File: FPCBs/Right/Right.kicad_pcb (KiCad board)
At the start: 2 copper layers, 61.5 x 89.2 mm, 23 parts, among them J1 PCB, J5 2nd Focus+Shutter, J6 Conn_01x03_Pin, SW1 Mode Dial, SW2 ON/OFF, SW3 Focus+Shutter, SW4 Focus+Shutter, SW6 ON/OFF, U1 SG-105, U2 SG-105

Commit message: Fix the buttons pins
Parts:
- removed F1: Fuse, Leica-G9ii:R_2x1mm
- added R9: 5k, Leica-G9ii:R_2x1mm, F.Cu at (121.8, 114.5)
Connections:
- RV1 pad 2: Net-(J1-Pin_35) -> Net-(J1-Pin_34)
- RV1 pad 3: Net-(J1-Pin_34) -> Net-(J1-Pin_35)
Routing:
- net Net-(J1-Pin_34): track 83.1 -> 87.0 mm
- net Net-(J1-Pin_35): track 85.7 -> 83.5 mm
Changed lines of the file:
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@@
 		)
 	)
+	(footprint "Leica-G9ii:R_2x1mm"
+		(layer "F.Cu")
+		(at 121.81 114.5 90)
+		(descr "Resistor SMD 0603 (1608 Metric), square (rectangular) end terminal, IPC-7351 nominal, (Body size source: IPC-SM-782 page 72, https://www.pcb-3d.com/wordpress/wp-content/uploads/ipc-sm-782a_amendment_1_and_2.pdf), generated with kicad-footprint-generator")
+		(tags "resistor")
+		(property "Reference" "R9"
+			(at 0 -1.43 90)
+			(layer "F.SilkS")
+			(hide yes)
+			(effects
+				(font
+					(size 1 1)
+					(thickness 0.15)
+				)
+			)
+		)
+		(property "Value" "5k"
+			(at 0 1.43 90)
+			(layer "F.Fab")
+			(effects
+				(font
+					(size 1 1)
+					(thickness 0.15)
+				)
+			)
+		)
+		(property "Datasheet" "~"
+			(at 0 0 90)
+			(layer "F.Fab")
+			(hide yes)
+			(effects
+				(font
+					(size 1.27 1.27)
+					(thickness 0.15)
+				)
+			)
+		)
+		(property "Description" "Resistor"
+			(at 0 0 90)
+			(layer "F.Fab")
+			(hide yes)
+			(effects
+				(font
+					(size 1.27 1.27)
+					(thickness 0.15)
+				)
+			)
+		)
+		(property ki_fp_filters "R_*")
+		(sheetname "/")
+		(sheetfile "Right.kicad_sch")
+		(attr smd)
+		(fp_rect
+			(start -1 -0.5)
+			(end 1 0.5)
+			(stroke
+				(width 0.05)
+				(type solid)
+			)
+			(fill no)
+			(layer "F.CrtYd")
+		)
+		(fp_line
+			(start 0.8 -0.4125)
+			(end 0.8 0.4125)
+			(stroke
+				(width 0.1)
+				(type solid)
+			)
+			(layer "F.Fab")
+		)
+		(fp_line
+			(start -0.8 -0.4125)
+			(end 0.8 -0.4125)
+			(stroke
+				(width 0.1)
+				(type solid)
+			)
+			(layer "F.Fab")
+		)
+		(fp_line
+			(start 0.8 0.4125)
+			(end -0.8 0.4125)
+			(stroke
+				(width 0.1)
+				(type solid)
+			)
+			(layer "F.Fab")
+		)
+		(fp_line
+			(start -0.8 0.4125)
+			(end -0.8 -0.4125)
+			(stroke
+				(width 0.1)
+				(type solid)
+			)
+			(layer "F.Fab")
+		)
+		(fp_text user "${REFERENCE}"
+			(at 3.42 0 90)
+			(layer "F.Fab")
+			(effects
+				(font
+					(size 0.4 0.4)
+					(thickness 0.06)
+				)
+			)
+		)
+		(pad "" smd roundrect
+			(at -0.6 0 90)
+			(size 0.6 0.8)
+			(layers "F.Mask" "F.Paste")
+			(roundrect_rratio 0.25)
+		)
+		(pad "" smd roundrect
+			(at 0.61 0 90)
+			(size 0.6 0.8)
+			(layers "F.Mask" "F.Paste")
+			(roundrect_rratio 0.25)
+		)
+		(pad "1" smd roundrect
+			(at -0.6 0 90)
+			(size 0.8 1)
+			(layers "F.Cu")
+			(roundrect_rratio 0.25)
+			(net 6 "Net-(J1-Pin_31)")
+			(pintype "passive")
+		)
+		(pad "2" smd roundrect
+			(at 0.6 0 90)
+			(size 0.8 1)
+			(layers "F.Cu")
+			(roundrect_rratio 0.25)
+			(net 5 "Net-(BT1-+)")
+			(pintype "passive")
+		)
+		(embedded_fonts no)
+		(model "${KICAD9_3DMODEL_DIR}/Resistor_SMD.3dshapes/R_0603_1608Metric.step"
+			(offset
+				(xyz 0 0 0)
+			)
+			(scale
+				(xyz 1 1 1)
+			)
+			(rotate
+				(xyz 0 0 0)
+			)
+		)
+	)
 	(footprint "Leica-G9ii:Battery_Cell"
 		(layer "F.Cu")
@@
 		)
 	)
-	(footprint "Leica-G9ii:R_2x1mm"
-		(layer "F.Cu")
-		(at 121.82 114.47 90)
-		(descr "Resistor SMD 0603 (1608 Metric), square (rectangular) end terminal, IPC-7351 nominal, (Body size source: IPC-SM-782 page 72, https://www.pcb-3d.com/wordpress/wp-content/uploads/ipc-sm-782a_amendment_1_and_2.pdf), generated with kicad-footprint-generator")
-		(tags "resistor")
-		(property "Reference" "F1"
-			(at 0 -1.43 90)
-			(layer "F.SilkS")
-			(hide yes)
-			(effects
-				(font
-					(size 1 1)
-					(thickness 0.15)
-				)
-			)
-		)
-		(property "Value" "Fuse"
-			(at 0 1.43 90)
-			(layer "F.Fab")
-			(effects
-				(font
-					(size 1 1)
-					(thickness 0.15)
-				)
-			)
-		)
-		(property "Datasheet" "~"
-			(at 0 0 90)
-			(layer "F.Fab")
-			(hide yes)
-			(effects
-				(font
-					(size 1.27 1.27)
-					(thickness 0.15)
-				)
-			)
-		)
-		(property "Description" "Fuse"
-			(at 0 0 90)
-			(layer "F.Fab")
-			(hide yes)
-			(effects
-				(font
-					(size 1.27 1.27)
-					(thickness 0.15)
-				)
-			)
-		)
-		(property ki_fp_filters "*Fuse*")
-		(sheetname "/")
-		(sheetfile "Right.kicad_sch")
-		(attr smd)
-		(fp_rect
-			(start -1 -0.5)
-			(end 1 0.5)
-			(stroke
-				(width 0.05)
-				(type solid)
-			)
-			(fill no)
-			(layer "F.CrtYd")
-		)
-		(fp_line
-			(start 0.8 -0.4125)
-			(end 0.8 0.4125)
-			(stroke
-				(width 0.1)
-				(type solid)
-			)
-			(layer "F.Fab")
-		)
-		(fp_line
-			(start -0.8 -0.4125)
-			(end 0.8 -0.4125)
-			(stroke
-				(width 0.1)
-				(type solid)
-			)
-			(layer "F.Fab")
-		)
-		(fp_line
-			(start 0.8 0.4125)
-			(end -0.8 0.4125)
-			(stroke
-				(width 0.1)
-				(type solid)
-			)
-			(layer "F.Fab")
-		)
-		(fp_line
-			(start -0.8 0.4125)
-			(end -0.8 -0.4125)
-			(stroke
-				(width 0.1)
-				(type solid)
-			)
-			(layer "F.Fab")
-		)
-		(fp_text user "${REFERENCE}"
-			(at 3.42 0 90)
-			(layer "F.Fab")
-			(effects
-				(font
-					(size 0.4 0.4)
-					(thickness 0.06)
-				)
-			)
-		)
-		(pad "" smd roundrect
-			(at -0.6 0 90)
-			(size 0.6 0.8)
-			(layers "F.Mask" "F.Paste")
-			(roundrect_rratio 0.25)
-		)
-		(pad "" smd roundrect
-			(at 0.61 0 90)
-			(size 0.6 0.8)
-			(layers "F.Mask" "F.Paste")
-			(roundrect_rratio 0.25)
-		)
-		(pad "1" smd roundrect
-			(at -0.6 0 90)
-			(size 0.8 1)
-			(layers "F.Cu")
-			(roundrect_rratio 0.25)
-			(net 6 "Net-(J1-Pin_31)")
-			(pintype "passive")
-		)
-		(pad "2" smd roundrect
-			(at 0.6 0 90)
-			(size 0.8 1)
-			(layers "F.Cu")
-			(roundrect_rratio 0.25)
-			(net 5 "Net-(BT1-+)")
-			(pintype "passive")
-		)
-		(embedded_fonts no)
-		(model "${KICAD9_3DMODEL_DIR}/Resistor_SMD.3dshapes/R_0603_1608Metric.step"
-			(offset
-				(xyz 0 0 0)
-			)
-			(scale
-				(xyz 1 1 1)
-			)
-			(rotate
-				(xyz 0 0 0)
-			)
-		)
-	)
 	(footprint "Leica-G9ii:2nd_dial"
 		(layer "F.Cu")
@@
 			(size 1.4 1.6)
 			(layers "F.Cu")
-			(net 28 "Net-(J1-Pin_35)")
+			(net 29 "Net-(J1-Pin_34)")
 			(pinfunction "2")
 			(pintype "passive")
@@
 			(size 1.4 1.6)
 			(layers "F.Cu")
-			(net 29 "Net-(J1-Pin_34)")
+			(net 28 "Net-(J1-Pin_35)")
 			(pinfunction "3")
 			(pintype "passive")
@@
 	)
 	(segment
-		(start 115.625 104.35)
-		(end 115.625 106.715)
+		(start 121.82 113.89)
+		(end 121.81 113.9)
+		(width 0.25)
+		(layer "F.Cu")
+		(net 5)
+	)
+	(segment
+		(start 115.625 106.715)
+		(end 121.82 112.91)
 		(width 0.25)
 		(layer "F.Cu")
@@
 	)
 	(segment
-		(start 115.625 106.715)
-		(end 121.82 112.91)
+		(start 115.625 104.35)
+		(end 115.625 106.715)
 		(width 0.25)
 		(layer "F.Cu")
@@
 	(segment
 		(start 121.82 112.91)
-		(end 121.82 113.87)
+		(end 121.82 113.89)
 		(width 0.25)
 		(layer "F.Cu")
@@
 	)
 	(segment
-		(start 121.81 124.69)
-		(end 121.81 115.1)
-		(width 0.25)
-		(layer "F.Cu")
-		(net 6)
-	)
-	(segment
 		(start 117.55 128.95)
 		(end 121.81 124.69)
@@
 	)
 	(segment
+		(start 121.81 124.69)
+		(end 121.81 115.1)
+		(width 0.25)
+		(layer "F.Cu")
+		(net 6)
+	)
+	(segment
 		(start 106.23 116.12)
 		(end 104.14 118.21)
@@
 	)
 	(segment
-		(start 119.365 129.685)
-		(end 140.53 108.52)
+		(start 119.3 129.75)
+		(end 141.93 107.12)
 		(width 0.14)
 		(layer "F.Cu")
@@
 	)
 	(segment
-		(start 119.3 129.75)
-		(end 119.365 129.685)
+		(start 119.3 179.82)
+		(end 119.3 129.75)
 		(width 0.14)
 		(layer "F.Cu")
@@
 	)
 	(segment
-		(start 145.05 107.83)
-		(end 145.05 107.12)
+		(start 141.93 107.12)
+		(end 143.23 107.12)
 		(width 0.14)
 		(layer "F.Cu")
@@
 	)
 	(segment
-		(start 140.53 108.52)
-		(end 144.36 108.52)
+		(start 118.98 129.645)
+		(end 142.565 106.06)
 		(width 0.14)
 		(layer "F.Cu")
-		(net 28)
+		(net 29)
 	)
 	(segment
-		(start 119.3 179.82)
-		(end 119.3 129.75)
+		(start 144.76 106.06)
+		(end 145.05 106.35)
 		(width 0.14)
 		(layer "F.Cu")
-		(net 28)
+		(net 29)
 	)
 	(segment
-		(start 144.36 108.52)
-		(end 145.05 107.83)
+		(start 142.565 106.06)
+		(end 144.76 106.06)
 		(width 0.14)
 		(layer "F.Cu")
-		(net 28)
+		(net 29)
 	)
 	(segment
-		(start 118.98 179.18)
-		(end 118.98 129.645)
+		(start 145.05 107.83)
+		(end 145.05 107.12)
 		(width 0.14)
 		(layer "F.Cu")
@@
 	)
 	(segment
-		(start 141.505 107.12)
-		(end 143.23 107.12)
+		(start 118.98 179.18)
+		(end 118.98 129.645)
 		(width 0.14)
 		(layer "F.Cu")
@@
 	)
 	(segment
-		(start 118.98 129.645)
-		(end 141.505 107.12)
+		(start 145.05 106.35)
+		(end 145.05 107.12)
 		(width 0.14)
 		(layer "F.Cu")

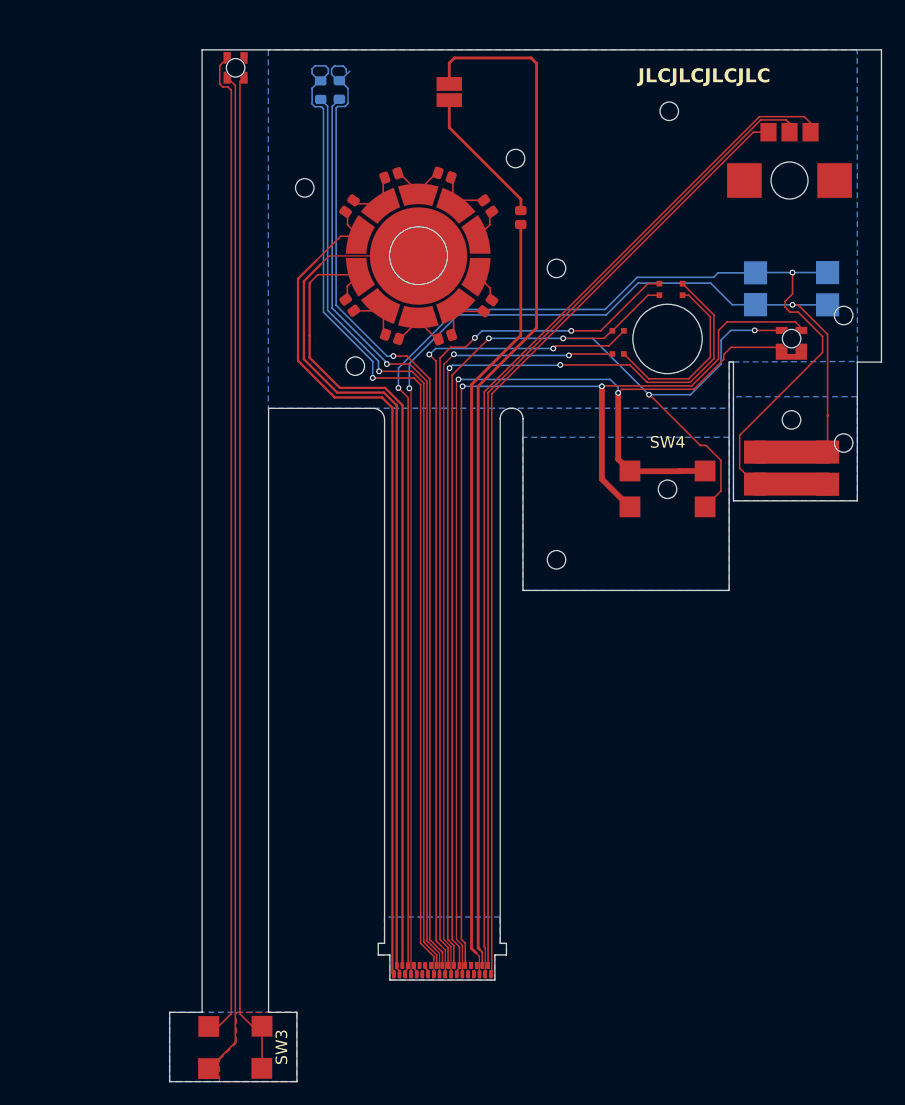
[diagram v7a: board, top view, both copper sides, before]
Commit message: Move fpc to left
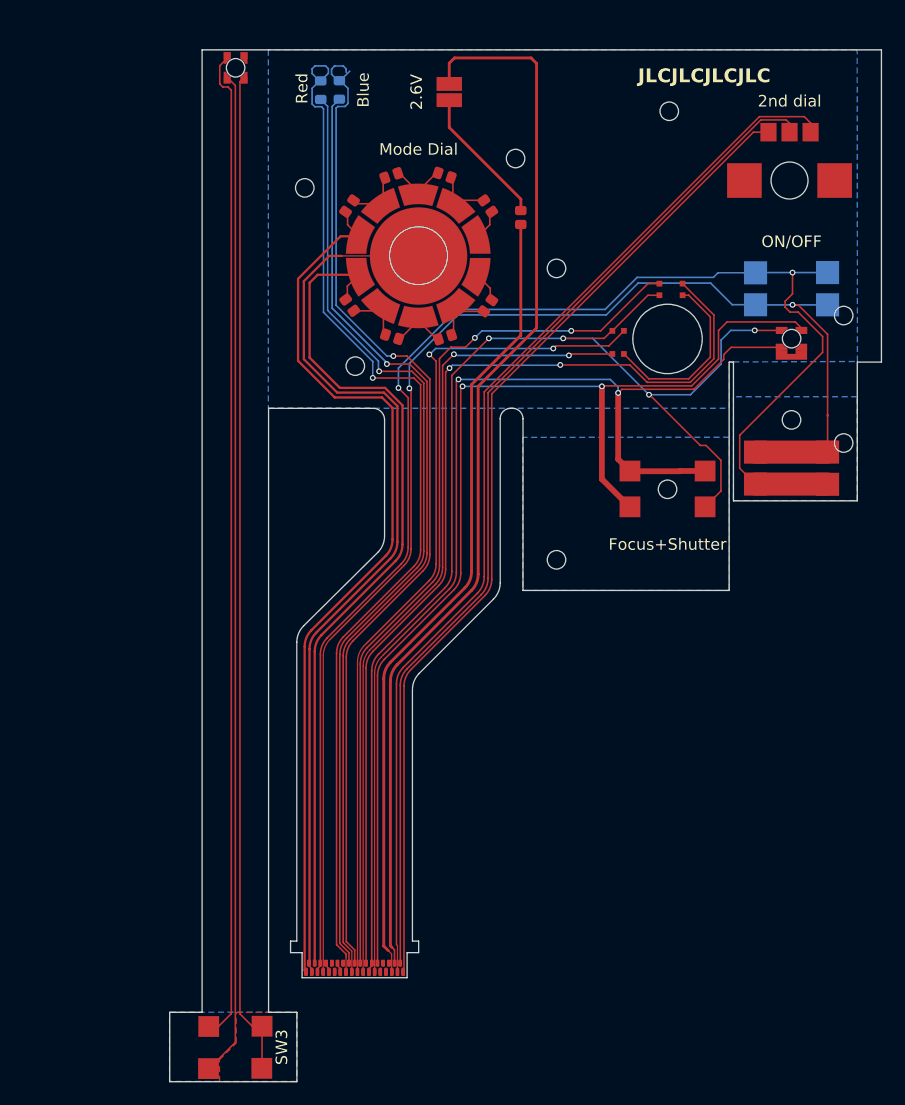
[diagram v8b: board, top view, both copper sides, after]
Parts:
- moved J1 7.59 mm to (107.4, 178.3)
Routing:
- net Net-(J1-Pin_2): track 73.1 -> 75.9 mm
- net Net-(J1-Pin_1): track 75.4 -> 78.1 mm
- net Net-(J1-Pin_5): track 123.3 -> 126.0 mm
- net Net-(J1-Pin_7): track 113.3 -> 116.1 mm
- net Net-(J1-Pin_35): track 83.5 -> 86.2 mm
- net Net-(J1-Pin_34): track 87.0 -> 89.7 mm
- net Net-(J1-Pin_4): track 71.8 -> 74.6 mm
- net Net-(J1-Pin_33): track 89.5 -> 92.2 mm
- net Net-(BT1--): track 90.0 -> 92.7 mm
- net Net-(J1-Pin_31): track 66.9 -> 69.6 mm
- net Net-(J1-Pin_26): track 95.3 -> 97.9 mm
- net Net-(D1-K): track 88.5 -> 91.0 mm
- net Net-(D1-A): track 80.7 -> 83.2 mm
- net Net-(D2-A): track 80.9 -> 83.4 mm
- net Net-(D2-K): track 86.9 -> 89.3 mm
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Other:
- outline, holes or cut-outs redrawn
